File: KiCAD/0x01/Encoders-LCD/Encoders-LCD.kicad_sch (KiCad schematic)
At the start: 22 parts, among them J1 I2C_Conn, J2 Btn_conn, J3 DSP-L, J4 DSP-R, SW1 SW_Push_LED, SW2 RotaryEncoder_Switch, SW3 RotaryEncoder_Switch, SW4 RotaryEncoder_Switch, U1 UC1, U2 UC2, U3 UC3

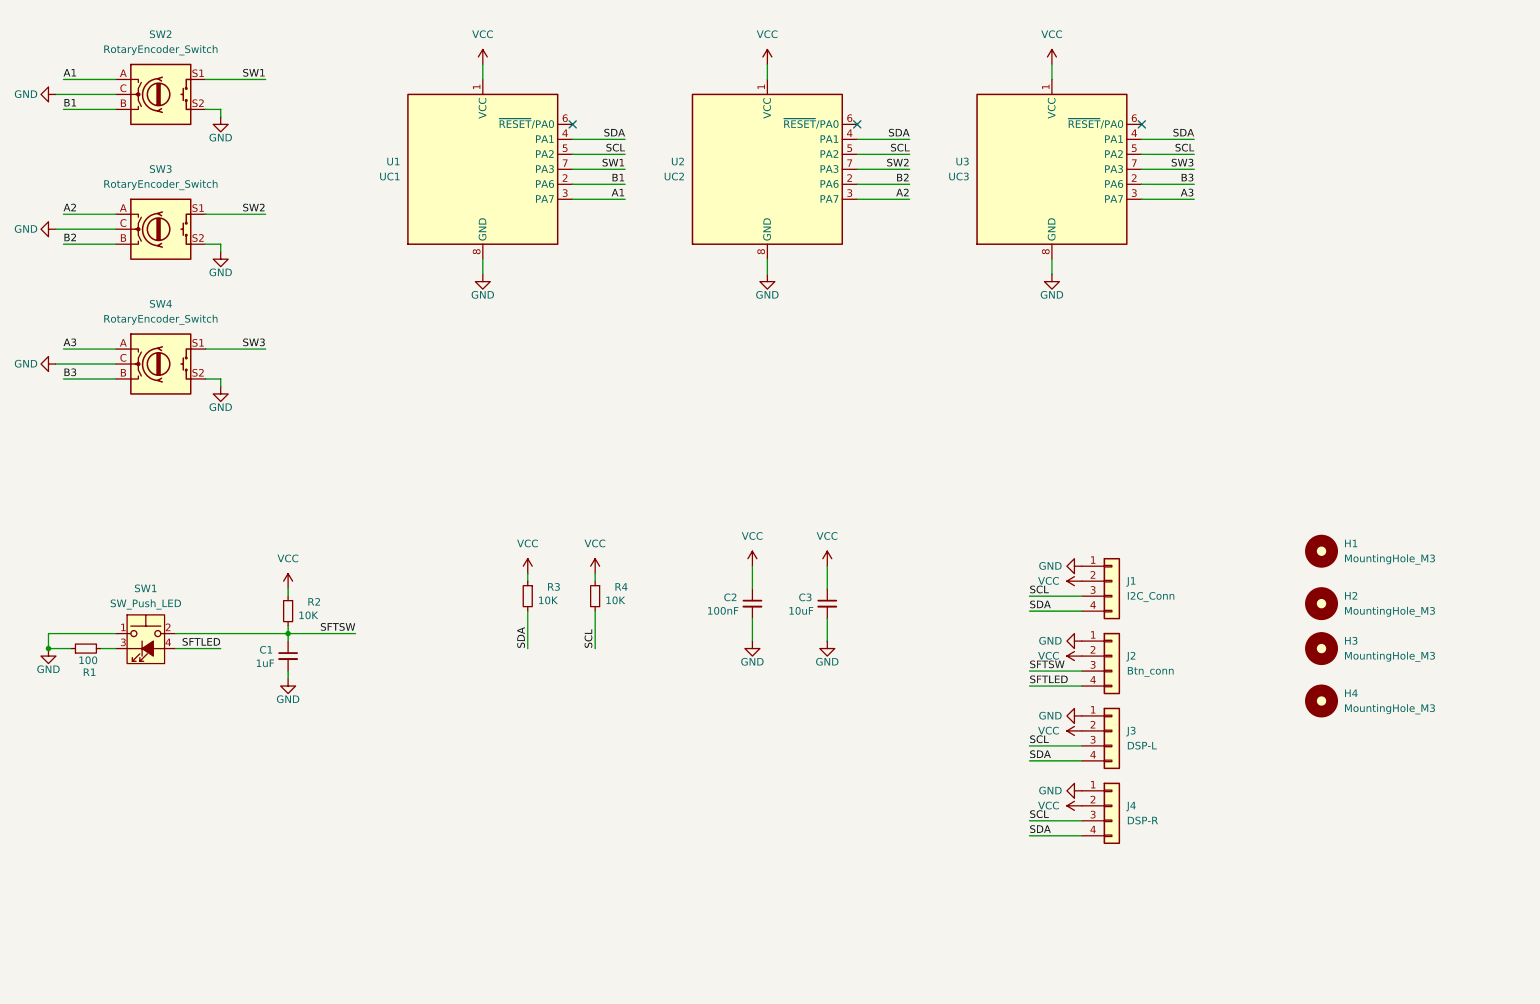
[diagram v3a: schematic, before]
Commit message: use 74hc165d with rotary encoders
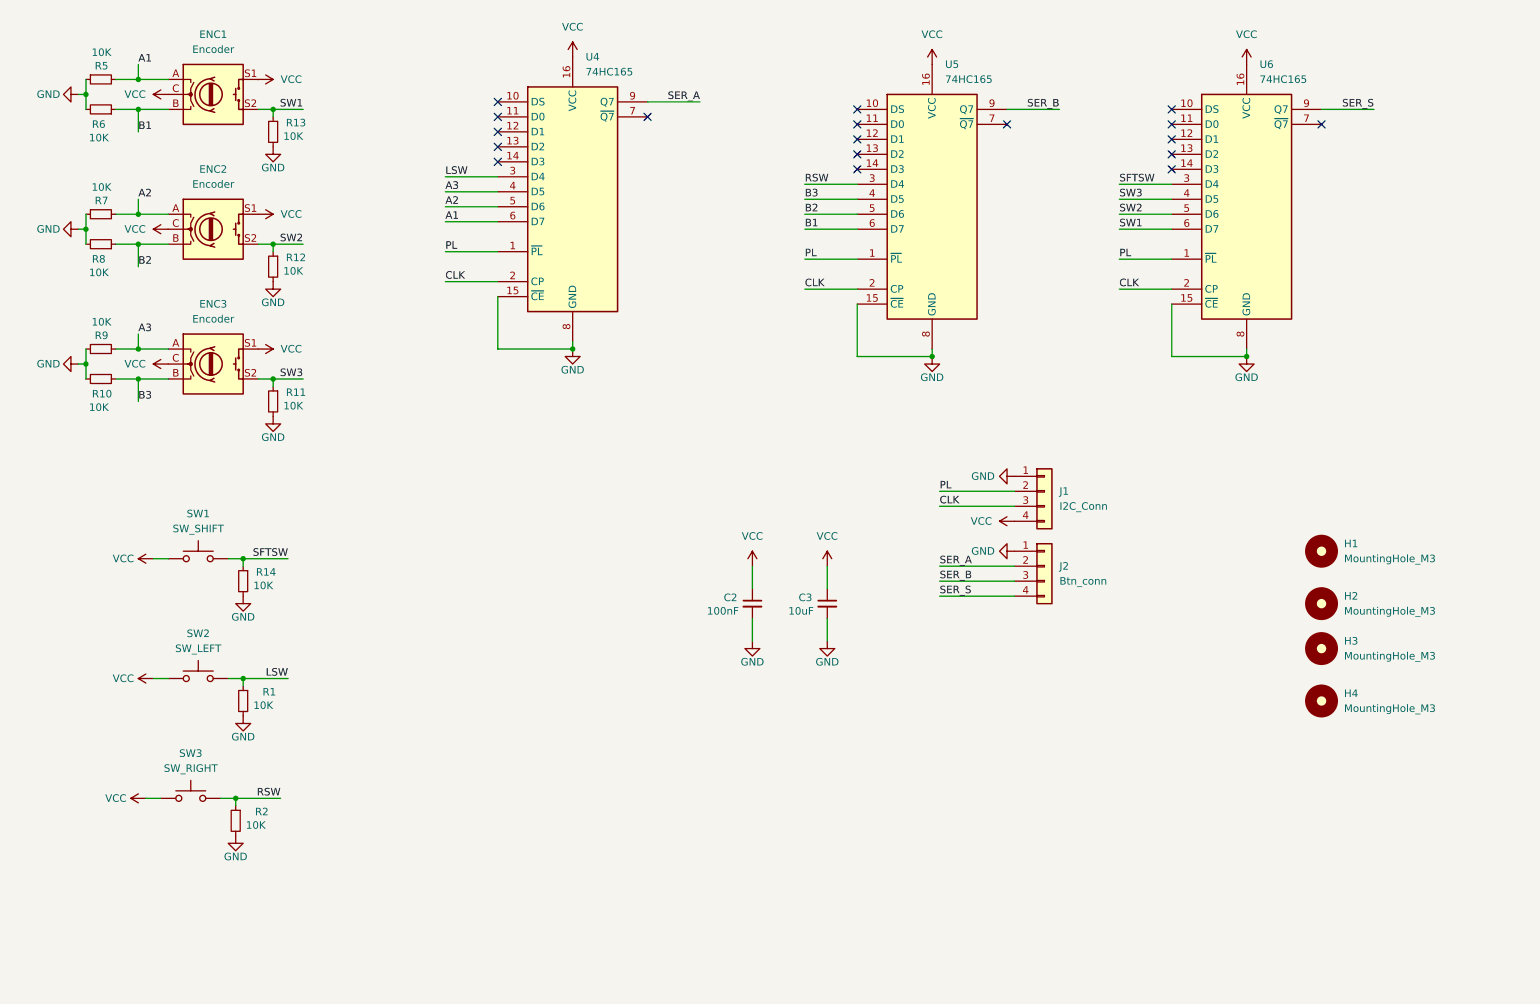
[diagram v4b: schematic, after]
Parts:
- removed C1: 1uF, Capacitor_SMD:C_0805_2012Metric_Pad1.18x1.45mm_HandSolder, symbol Device:C_Small
- removed J3: DSP-L, Connector_PinHeader_2.54mm:PinHeader_1x04_P2.54mm_Vertical, symbol Connector_Generic:Conn_01x04
- removed J4: DSP-R, Connector_PinHeader_2.54mm:PinHeader_1x04_P2.54mm_Vertical, symbol Connector_Generic:Conn_01x04
- removed R3, R4: 10K, PCM_Resistor_SMD_AKL:R_0805_2012Metric_Pad1.20x1.40mm_HandSolder, symbol Device:R_Small
- removed SW1: SW_Push_LED, led-sw:led switch, symbol Switch:SW_Push_LED
- removed U1: UC1, Package_SO:SOIC-8_3.9x4.9mm_P1.27mm, symbol MCU_Microchip_ATtiny:ATtiny412-SS
- removed U2: UC2, Package_SO:SOIC-8_3.9x4.9mm_P1.27mm, symbol MCU_Microchip_ATtiny:ATtiny412-SS
- removed U3: UC3, Package_SO:SOIC-8_3.9x4.9mm_P1.27mm, symbol MCU_Microchip_ATtiny:ATtiny412-SS
- added R10, R11, R12, R13, R14, R5, R6, R7, R8, R9: 10K, Capacitor_SMD:C_0805_2012Metric_Pad1.18x1.45mm_HandSolder, symbol Device:R_Small
- added SW1: SW_SHIFT, Button_Switch_THT:SW_PUSH_6mm_H4.3mm, symbol Switch:SW_Push
- added SW2: SW_LEFT, Button_Switch_THT:SW_PUSH_6mm_H4.3mm, symbol Switch:SW_Push
- added SW3: SW_RIGHT, Button_Switch_THT:SW_PUSH_6mm_H4.3mm, symbol Switch:SW_Push
- added U4, U5, U6: 74HC165, Package_SO:SOIC-16_3.9x9.9mm_P1.27mm, symbol 74xx:74HC165
- ENC1: renamed from SW2; value RotaryEncoder_Switch -> Encoder
- ENC2: renamed from SW3; value RotaryEncoder_Switch -> Encoder
- ENC3: renamed from SW4; value RotaryEncoder_Switch -> Encoder
- R1: value 100 -> 10K; footprint PCM_Resistor_SMD_AKL:R_0805_2012Metric_Pad1.20x1.40mm_HandSolder -> Capacitor_SMD:C_0805_2012Metric_Pad1.18x1.45mm_HandSolder
- R2: footprint PCM_Resistor_SMD_AKL:R_0805_2012Metric_Pad1.20x1.40mm_HandSolder -> Capacitor_SMD:C_0805_2012Metric_Pad1.18x1.45mm_HandSolder
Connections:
- net SDA is gone; now on net VCC: J1.4 (Pin_4)
- net A1: now also R5.2, U4.6 (D7)
- net A2: now also R7.2, U4.5 (D6)
- net A3: now also R9.2, U4.4 (D5)
- net B1: now also R6.1, U5.6 (D7)
- net B2: now also R8.1, U5.5 (D6)
- net B3: now also R10.1, U5.4 (D5)
- net GND: now also R1.2, R2.2, R10.2, R11.2, R12.2, R13.2, R14.2, R5.1, R6.2, R7.1, R8.2, R9.1, U4.15 (~{CE}), U4.8 (GND), U5.15 (~{CE}), U5.8 (GND), U6.15 (~{CE}), U6.8 (GND); no longer ENC1.C, ENC1.S2, ENC2.C, ENC2.S2, ENC3.C, ENC3.S2, R1.1
- net SFTSW: now also R14.1, SW1.2, U6.3 (D4); no longer J2.3 (Pin_3), R2.2
- net SW1: now also ENC1.S2, R13.1, U6.6 (D7); no longer ENC1.S1
- net SW2: now also ENC2.S2, R12.1, U6.5 (D6); no longer ENC2.S1
- net SW3: now also ENC3.S2, R11.1, U6.4 (D5); no longer ENC3.S1
- net VCC: now also ENC1.C, ENC1.S1, ENC2.C, ENC2.S1, ENC3.C, ENC3.S1, SW1.1, SW2.1, SW3.1, U4.16 (VCC), U5.16 (VCC), U6.16 (VCC); no longer J1.2 (Pin_2), J2.2 (Pin_2), R2.1
- net SCL renamed CLK
- net CLK: now also U4.2 (CP), U5.2 (CP), U6.2 (CP)
- net SFTLED renamed SER_S
- net SER_S: now also U6.9 (Q7)
- new net LSW: R1.1, SW2.2, U4.3 (D4)
- new net PL: J1.2 (Pin_2), U4.1 (~{PL}), U5.1 (~{PL}), U6.1 (~{PL})
- new net RSW: R2.1, SW3.2, U5.3 (D4)
- new net SER_A: J2.2 (Pin_2), U4.9 (Q7)
- new net SER_B: J2.3 (Pin_3), U5.9 (Q7)
- no-connect marks 3 -> 18
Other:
- moved on the sheet: ENC1, ENC2, ENC3, J1, J2

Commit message: re-routing encoders pcb
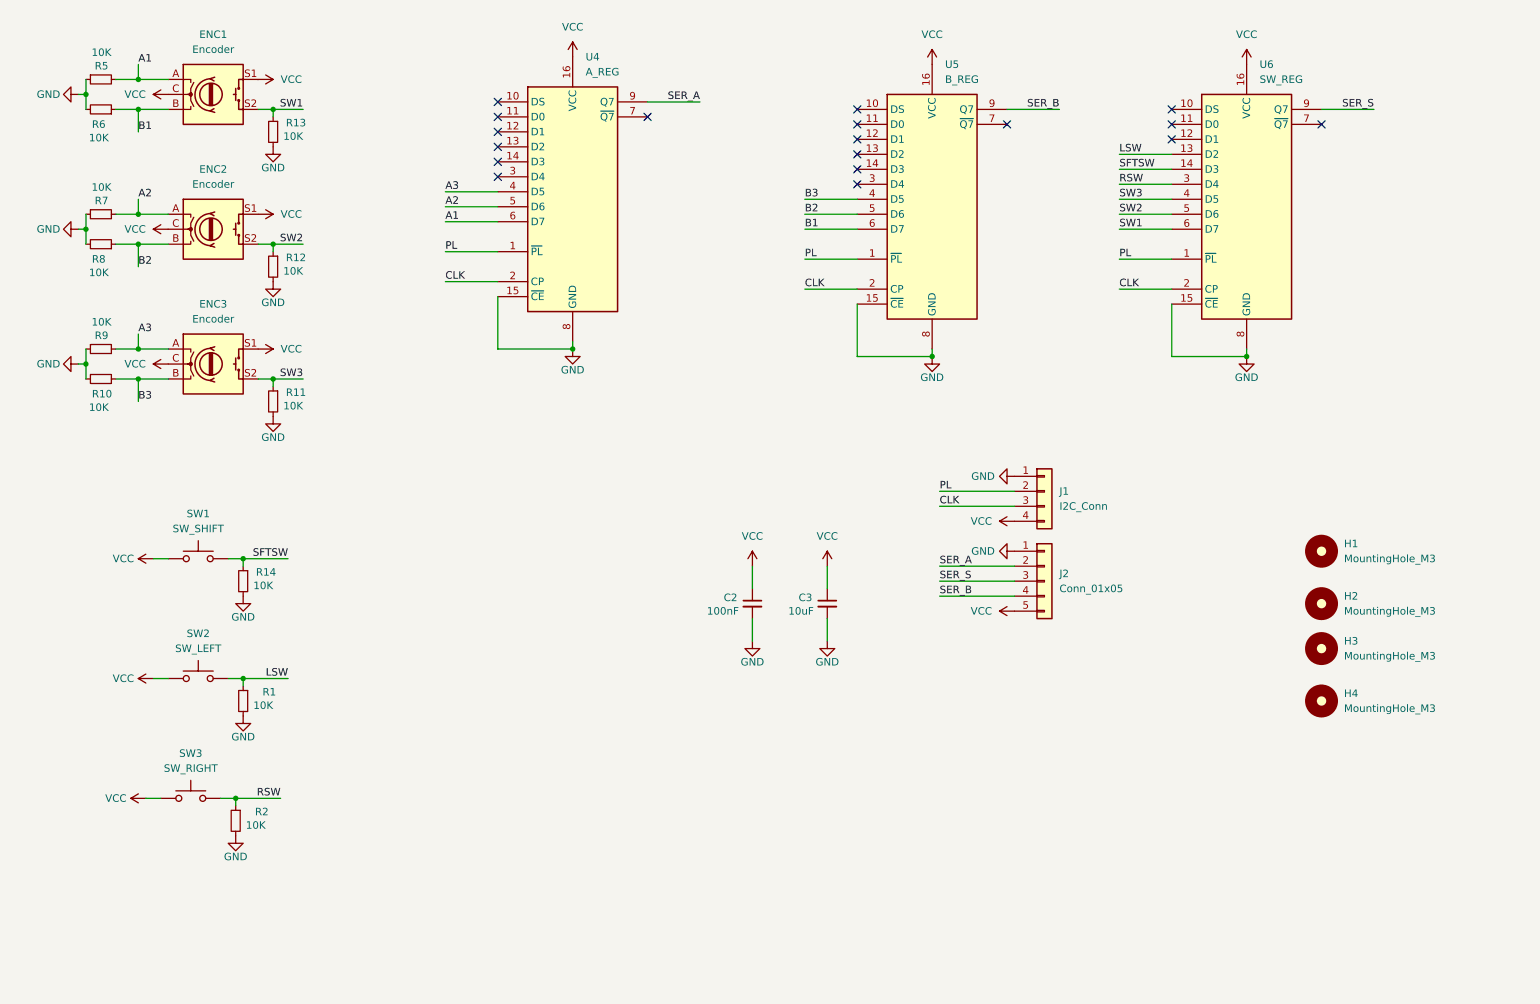
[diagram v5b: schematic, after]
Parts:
- removed J2: Btn_conn, Connector_Hirose:Hirose_DF13-04P-1.25DS_1x04_P1.25mm_Horizontal, symbol Connector_Generic:Conn_01x04
- added J2: Conn_01x05, Connector_PinHeader_2.54mm:PinHeader_1x05_P2.54mm_Vertical, symbol Connector_Generic:Conn_01x05
- J1: footprint Connector_Hirose:Hirose_DF13-04P-1.25DS_1x04_P1.25mm_Horizontal -> Connector_PinHeader_2.54mm:PinHeader_1x04_P2.54mm_Vertical
- U4: value 74HC165 -> A_REG
- U5: value 74HC165 -> B_REG
- U6: value 74HC165 -> SW_REG
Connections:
- net GND: now also J2.1 (Pin_1)
- net LSW: now also U6.13 (D2); no longer U4.3 (D4)
- net RSW: now also U6.3 (D4); no longer U5.3 (D4)
- net SER_A: now also J2.2 (Pin_2)
- net SER_B: now also J2.4 (Pin_4)
- net SER_S: now also J2.3 (Pin_3)
- net SFTSW: now also U6.14 (D3); no longer U6.3 (D4)
- net VCC: now also J2.5 (Pin_5)
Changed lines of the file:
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@@
 	)
 	(no_connect
-		(at 217.17 46.99)
+		(at 102.87 48.26)
 	)
 	(no_connect
-		(at 217.17 44.45)
+		(at 163.83 49.53)
 	)
 	(wire
@@
 	(wire
 		(pts
-			(xy 208.28 49.53) (xy 217.17 49.53)
+			(xy 208.28 46.99) (xy 217.17 46.99)
 		)
 		(stroke
@@
 	(wire
 		(pts
-			(xy 93.98 48.26) (xy 102.87 48.26)
+			(xy 208.28 44.45) (xy 217.17 44.45)
 		)
 		(stroke
@@
 	(wire
 		(pts
-			(xy 154.94 49.53) (xy 163.83 49.53)
+			(xy 208.28 49.53) (xy 217.17 49.53)
 		)
 		(stroke
@@
 	)
 	(label "SFTSW"
-		(at 208.28 49.53 0)
+		(at 208.28 46.99 0)
 		(effects
 			(font
@@
 	)
 	(label "SER_S"
-		(at 177.8 119.38 0)
+		(at 177.8 116.84 0)
 		(effects
 			(font
@@
 	)
 	(label "SER_B"
-		(at 177.8 116.84 0)
+		(at 177.8 119.38 0)
 		(effects
 			(font
@@
 	)
 	(label "LSW"
-		(at 93.98 48.26 0)
+		(at 208.28 44.45 0)
 		(effects
 			(font
@@
 	)
 	(label "RSW"
-		(at 154.94 49.53 0)
+		(at 208.28 49.53 0)
 		(effects
 			(font
@@
 			)
 		)
-		(property "Value" "74HC165"
+		(property "Value" "SW_REG"
 			(at 232.0641 31.75 0)
 			(effects
@@
 			)
 		)
-		(property "Value" "74HC165"
+		(property "Value" "A_REG"
 			(at 117.7641 30.48 0)
 			(effects
@@
 	)
 	(symbol
+		(lib_id "power:VCC")
+		(at 190.5 121.92 90)
+		(unit 1)
+		(exclude_from_sim no)
+		(in_bom yes)
+		(on_board yes)
+		(dnp no)
+		(fields_autoplaced yes)
+		(property "Reference" "#PWR012"
+			(at 194.31 121.92 0)
+			(effects
+				(font
+					(size 1.27 1.27)
+				)
+				(hide yes)
+			)
+		)
+		(property "Value" "VCC"
+			(at 186.69 121.9199 90)
+			(effects
+				(font
+					(size 1.27 1.27)
+				)
+				(justify left)
+			)
+		)
+		(property "Footprint" ""
+			(at 190.5 121.92 0)
+			(effects
+				(font
+					(size 1.27 1.27)
+				)
+				(hide yes)
+			)
+		)
+		(property "Datasheet" ""
+			(at 190.5 121.92 0)
+			(effects
+				(font
+					(size 1.27 1.27)
+				)
+				(hide yes)
+			)
+		)
+		(property "Description" "Power symbol creates a global label with name \"VCC\""
+			(at 190.5 121.92 0)
+			(effects
+				(font
+					(size 1.27 1.27)
+				)
+				(hide yes)
+			)
+		)
+		(pin "1"
+		)
+		(instances
+			(project "Encoders-LCD"
+				(path "/094609a0-ed7a-433b-8808-fc69fd09a73b"
+					(reference "#PWR012")
+					(unit 1)
+				)
+			)
+		)
+	)
+	(symbol
 		(lib_id "Connector_Generic:Conn_01x04")
 		(at 195.58 101.6 0)
@@
 			)
 		)
-		(property "Footprint" "Connector_Hirose:Hirose_DF13-04P-1.25DS_1x04_P1.25mm_Horizontal"
+		(property "Footprint" "Connector_PinHeader_2.54mm:PinHeader_1x04_P2.54mm_Vertical"
 			(at 195.58 101.6 0)
 			(effects
@@
 	)
 	(symbol
-		(lib_id "Connector_Generic:Conn_01x04")
-		(at 195.58 114.3 0)
+		(lib_id "Device:R_Small")
+		(at 35.56 31.75 90)
+		(mirror x)
 		(unit 1)
 		(exclude_from_sim no)
@@
 		(on_board yes)
 		(dnp no)
-		(fields_autoplaced yes)
-		(property "Reference" "J2"
-			(at 198.12 114.2999 0)
+		(property "Reference" "R5"
+			(at 36.83 29.464 90)
 			(effects
 				(font
@@
 			)
 		)
-		(property "Value" "Btn_conn"
-			(at 198.12 116.8399 0)
+		(property "Value" "10K"
+			(at 37.338 27.178 90)
 			(effects
 				(font
@@
 			)
 		)
-		(property "Footprint" "Connector_Hirose:Hirose_DF13-04P-1.25DS_1x04_P1.25mm_Horizontal"
-			(at 195.58 114.3 0)
+		(property "Footprint" "Capacitor_SMD:C_0805_2012Metric_Pad1.18x1.45mm_HandSolder"
+			(at 35.56 31.75 0)
 			(effects
 				(font
@@
 		)
 		(property "Datasheet" "~"
-			(at 195.58 114.3 0)
+			(at 35.56 31.75 0)
 			(effects
 				(font
@@
 			)
 		)
-		(property "Description" "Generic connector, single row, 01x04, script generated (kicad-library-utils/schlib/autogen/connector/)"
-			(at 195.58 114.3 0)
+		(property "Description" "Resistor, small symbol"
+			(at 35.56 31.75 0)
 			(effects
 				(font
@@
 			)
 		)
-		(pin "4"
-		)
-		(pin "3"
+		(pin "1"
 		)
 		(pin "2"
 		)
-		(pin "1"
-		)
 		(instances
 			(project "Encoders-LCD"
 				(path "/094609a0-ed7a-433b-8808-fc69fd09a73b"
-					(reference "J2")
+					(reference "R5")
 					(unit 1)
 				)
@@
 	)
 	(symbol
-		(lib_id "Device:R_Small")
-		(at 35.56 31.75 90)
-		(mirror x)
+		(lib_id "power:GND")
+		(at 64.77 66.04 0)
 		(unit 1)
 		(exclude_from_sim no)
@@
 		(on_board yes)
 		(dnp no)
-		(property "Reference" "R5"
-			(at 36.83 29.464 90)
+		(property "Reference" "#PWR035"
+			(at 64.77 72.39 0)
 			(effects
 				(font
 					(size 1.27 1.27)
 				)
-				(justify left)
+				(hide yes)
 			)
 		)
-		(property "Value" "10K"
-			(at 37.338 27.178 90)
+		(property "Value" "GND"
+			(at 64.77 69.596 0)
 			(effects
 				(font
 					(size 1.27 1.27)
 				)
-				(justify left)
 			)
 		)
-		(property "Footprint" "Capacitor_SMD:C_0805_2012Metric_Pad1.18x1.45mm_HandSolder"
-			(at 35.56 31.75 0)
+		(property "Footprint" ""
+			(at 64.77 66.04 0)
 			(effects
 				(font
@@
 			)
 		)
-		(property "Datasheet" "~"
-			(at 35.56 31.75 0)
+		(property "Datasheet" ""
+			(at 64.77 66.04 0)
 			(effects
 				(font
@@
 			)
 		)
-		(property "Description" "Resistor, small symbol"
-			(at 35.56 31.75 0)
+		(property "Description" "Power symbol creates a global label with name \"GND\" , ground"
+			(at 64.77 66.04 0)
 			(effects
 				(font
@@
 		(pin "1"
 		)
-		(pin "2"
-		)
 		(instances
 			(project "Encoders-LCD"
 				(path "/094609a0-ed7a-433b-8808-fc69fd09a73b"
-					(reference "R5")
+					(reference "#PWR035")
 					(unit 1)
 				)
@@
 	)
 	(symbol
-		(lib_id "power:GND")
-		(at 64.77 66.04 0)
+		(lib_id "Connector_Generic:Conn_01x05")
+		(at 195.58 116.84 0)
 		(unit 1)
 		(exclude_from_sim no)
@@
 		(on_board yes)
 		(dnp no)
-		(property "Reference" "#PWR035"
-			(at 64.77 72.39 0)
+		(fields_autoplaced yes)
+		(property "Reference" "J2"
+			(at 198.12 115.5699 0)
 			(effects
 				(font
 					(size 1.27 1.27)
 				)
-				(hide yes)
+				(justify left)
 			)
 		)
-		(property "Value" "GND"
-			(at 64.77 69.596 0)
+		(property "Value" "Conn_01x05"
+			(at 198.12 118.1099 0)
 			(effects
 				(font
 					(size 1.27 1.27)
 				)
+				(justify left)
 			)
 		)
-		(property "Footprint" ""
-			(at 64.77 66.04 0)
+		(property "Footprint" "Connector_PinHeader_2.54mm:PinHeader_1x05_P2.54mm_Vertical"
+			(at 195.58 116.84 0)
 			(effects
 				(font
@@
 			)
 		)
-		(property "Datasheet" ""
-			(at 64.77 66.04 0)
+		(property "Datasheet" "~"
+			(at 195.58 116.84 0)
 			(effects
 				(font
@@
 			)
 		)
-		(property "Description" "Power symbol creates a global label with name \"GND\" , ground"
-			(at 64.77 66.04 0)
+		(property "Description" "Generic connector, single row, 01x05, script generated (kicad-library-utils/schlib/autogen/connector/)"
+			(at 195.58 116.84 0)
 			(effects
 				(font
@@
 		(pin "1"
 		)
+		(pin "4"
+		)
+		(pin "3"
+		)
+		(pin "2"
+		)
+		(pin "5"
+		)
 		(instances
-			(project "Encoders-LCD"
+			(project ""
 				(path "/094609a0-ed7a-433b-8808-fc69fd09a73b"
-					(reference "#PWR035")
+					(reference "J2")
 					(unit 1)
 				)
@@
 			)
 		)
-		(property "Value" "74HC165"
+		(property "Value" "B_REG"
 			(at 178.7241 31.75 0)
 			(effects
